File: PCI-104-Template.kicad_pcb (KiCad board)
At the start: 2 copper layers, 95.9 x 90.2 mm, 6 parts, among them J1 Conn_02x30_Row_Letter_First, J2 Conn_02x30_Row_Letter_First

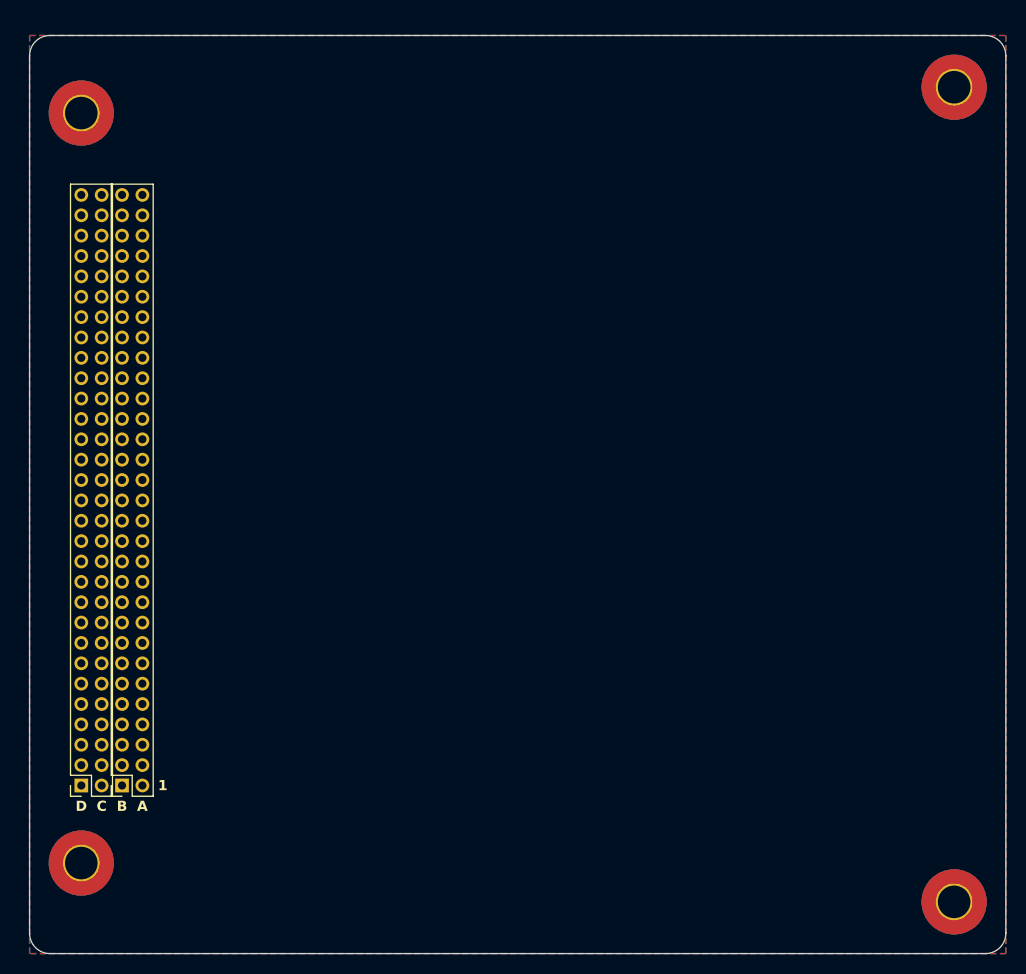
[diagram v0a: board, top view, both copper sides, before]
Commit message: Add holes for shroud locking pegs
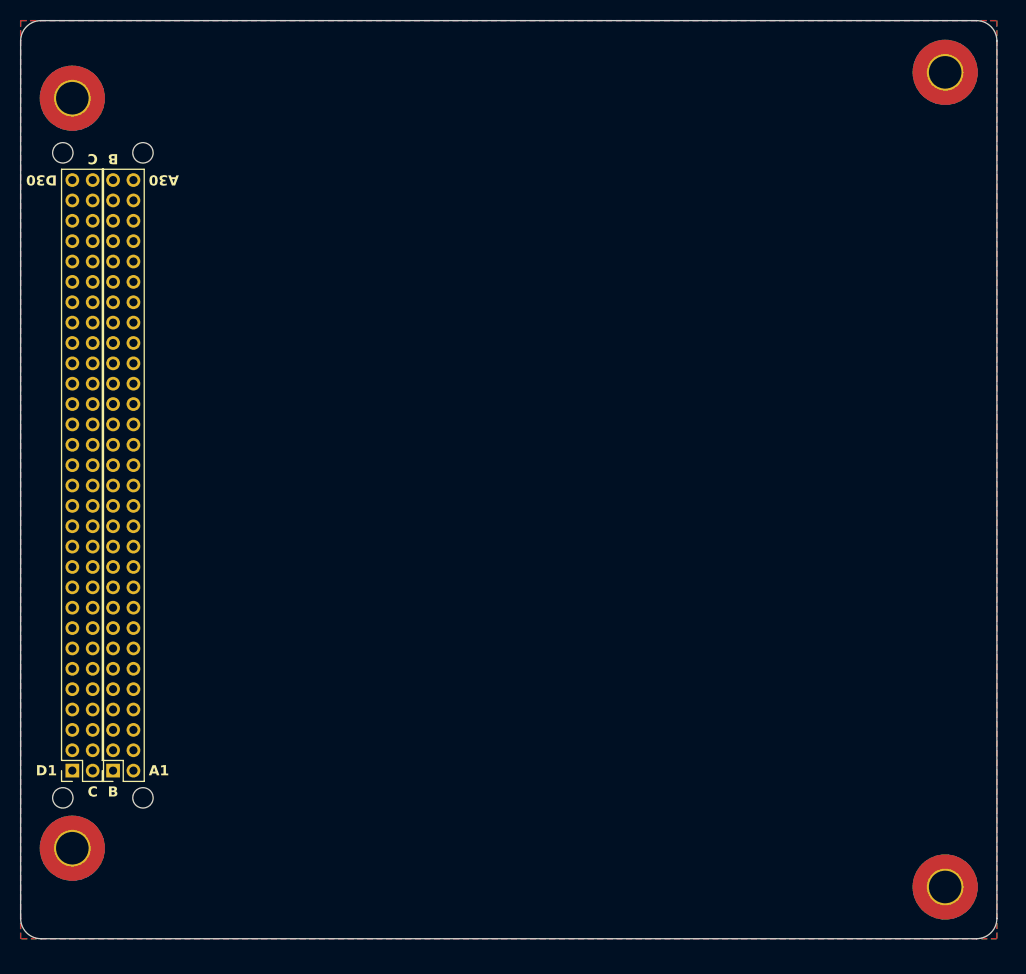
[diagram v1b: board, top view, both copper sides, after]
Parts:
- added H5: MountingHole, MountingHole:MountingHole_2mm, F.Cu at (54.1, 62.3)
- added H6: MountingHole, MountingHole:MountingHole_2mm, F.Cu at (61.9, 62.3)
- added H7: MountingHole, MountingHole:MountingHole_2mm, F.Cu at (54.1, 125.7)
- added H8: MountingHole, MountingHole:MountingHole_2mm, F.Cu at (61.9, 125.7)
- moved H3 1.70 mm to (55.0, 130.6)
- moved H1 1.70 mm to (55.0, 57.0)
- moved H2 1.70 mm to (140.7, 54.4)
- moved J1 1.70 mm to (59.0, 123.0)
- moved J2 1.70 mm to (55.0, 123.0)
- moved H4 1.70 mm to (140.7, 134.4)
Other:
- board text added: "A1"
- board text added: "A30"
- board text added: "D1"
- board text added: "D30"
- board text removed: "1"
- board text removed: "A"
- board text removed: "D"
